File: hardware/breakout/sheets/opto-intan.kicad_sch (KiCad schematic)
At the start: 43 parts, among them J46 Intan opto out: EVT_STROBE_IN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, J47 Intan opto out: BARCODE_INTAN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, J48 Intan opto out: RWD_CMD_INTAN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, J49 Intan opto out: RWD_DLVR_INTA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, J50 Intan opto out: STIM_TRIG_INT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, J51 Intan RHS stim status in (BNC), U63 TMR 1-0511, U64 ACSL-6400-00TE, U65 ACSL-6420-00TE, U75 SN74AHCT541PW

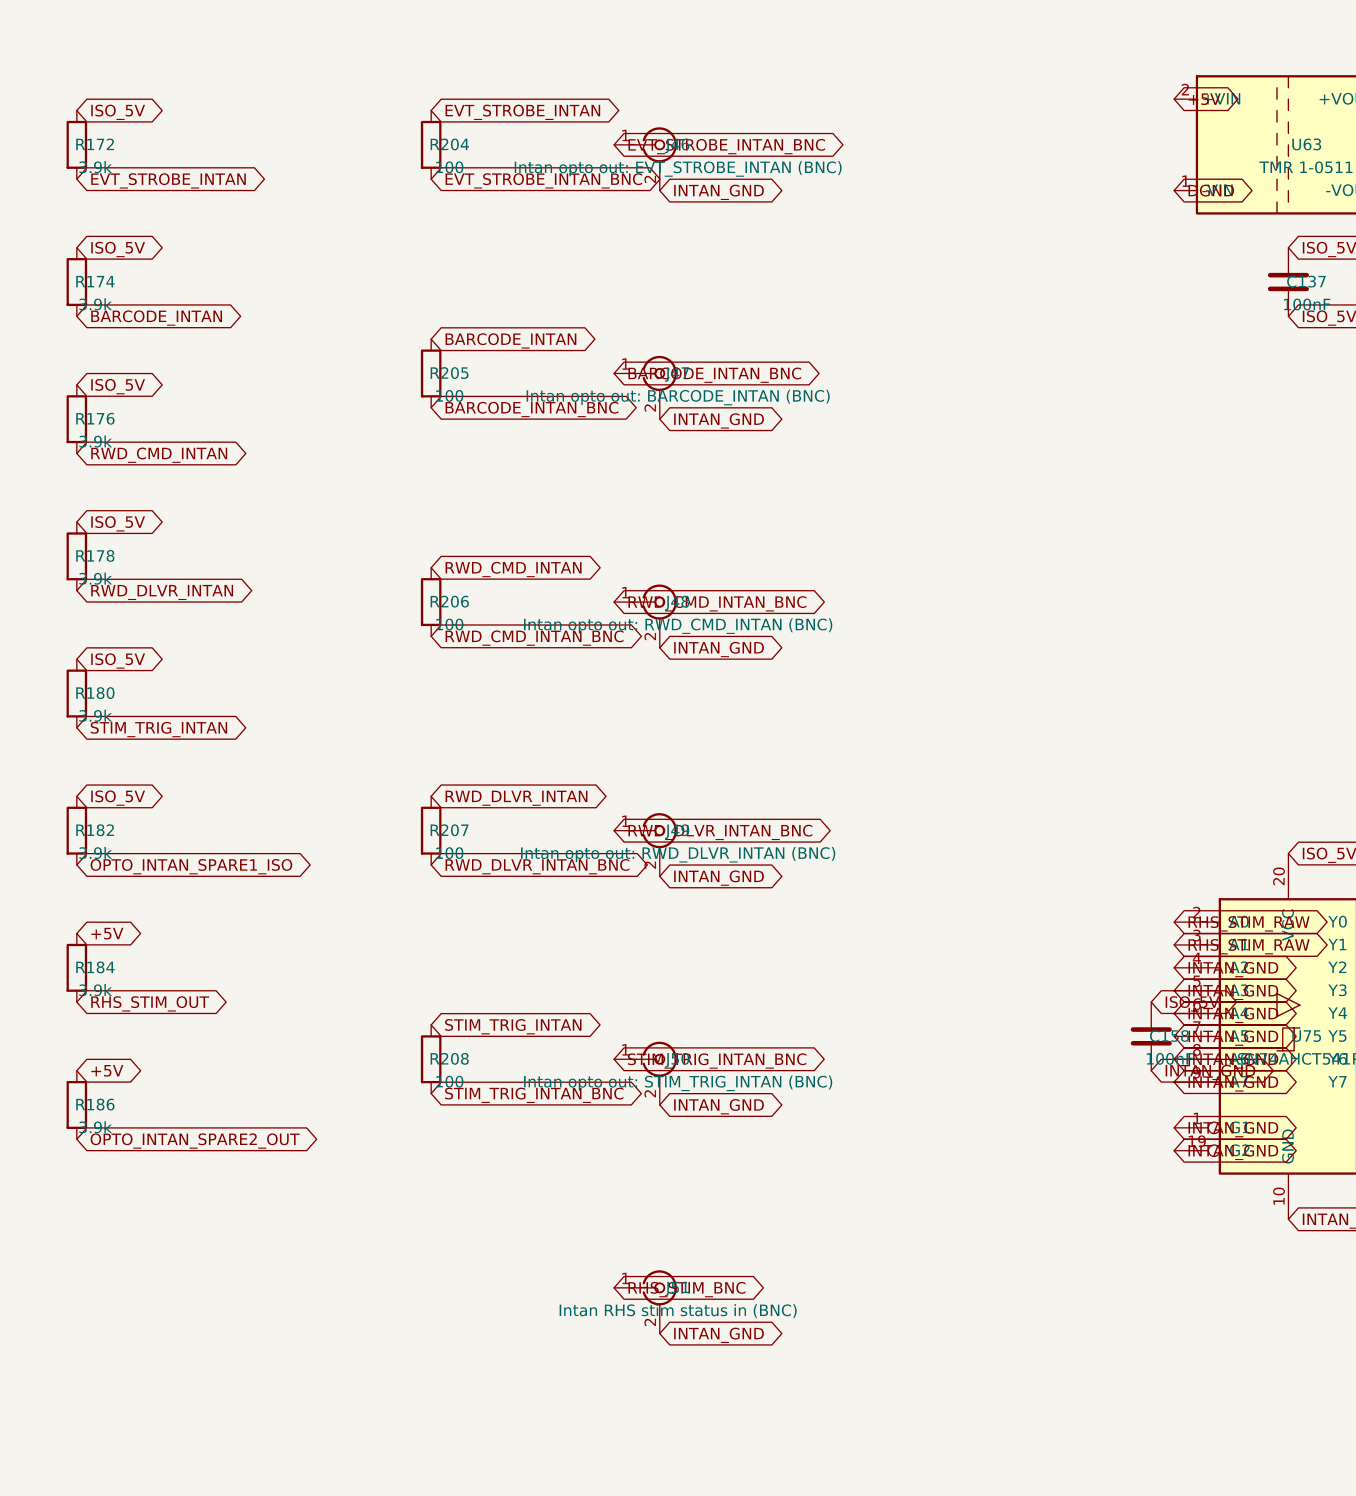
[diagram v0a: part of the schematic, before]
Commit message: fix(hardware): rebuild the connectors on their primary drawings (F6, R1, D3)
Audit step 5, the mechanical half. Three connectors changed, one of them a
fab-stopper, and none of it was visible to the netlist.

MDR68 (the fab-stopper). Rebuilt from MH drawing 3700-0121-01 rev 3.0. The
as-built footprint drilled contacts at 0.5 mm against a required 0.85 mm -- the
pins do not fit, so the board could not have been assembled -- and laid them out
as 2 rows at 2.84 mm where the drawing shows 4 staggered rows of 17 at 1.905 mm.
The 4-row stagger is what makes an 0.85 mm drill manufacturable at a 1.27 mm
mating pitch at all; the array now spans the drawing's own 41.91 mm exactly,
which is the arithmetic that confirms the reading. The claim made during the
audit that it had "no mounting holes at all" was wrong: it had two, Ø2.79 on
57.9 mm centres against the drawing's Ø2.77 on 57.93.

M12 (ruling R1). M12A_5_Panel is deleted, symbol and footprint and generator
function alike. Its contact geometry was sourced well -- IEC 61076-2-101
A-coding, cross-checked three ways -- and it made no difference, because the part
the design procures (Phoenix 1551833) terminates in AWG 22-20 wire and mounts
through the panel. It has no PCB tails, so no board-mount footprint of any
dimensions could have been right, and as built every cable insertion and every
3-4 N.m tightening loaded PCB pads directly. J1 is now a stock 5-way header where
those flying leads land; the connector stays in the order BOM as chassis
furniture.

BNC (F6). BNC_PanelMountable_Vertical puts the connector axis perpendicular to
the PCB -- a 9.65 mm barrel hole through the board -- so on a 430x240 mm board
lying flat in a 2U chassis all 31 barrels pointed at the lid rather than at the
panels. It also cost 5,654 mm2 of pad and 2,267 mm2 of removed copper on every
layer. Replaced by a right-angle dual jack built from Amphenol drawing 31-6575
rev A: 31 ports on 17 bodies, 3 spare ports, every shell still routed
individually.
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
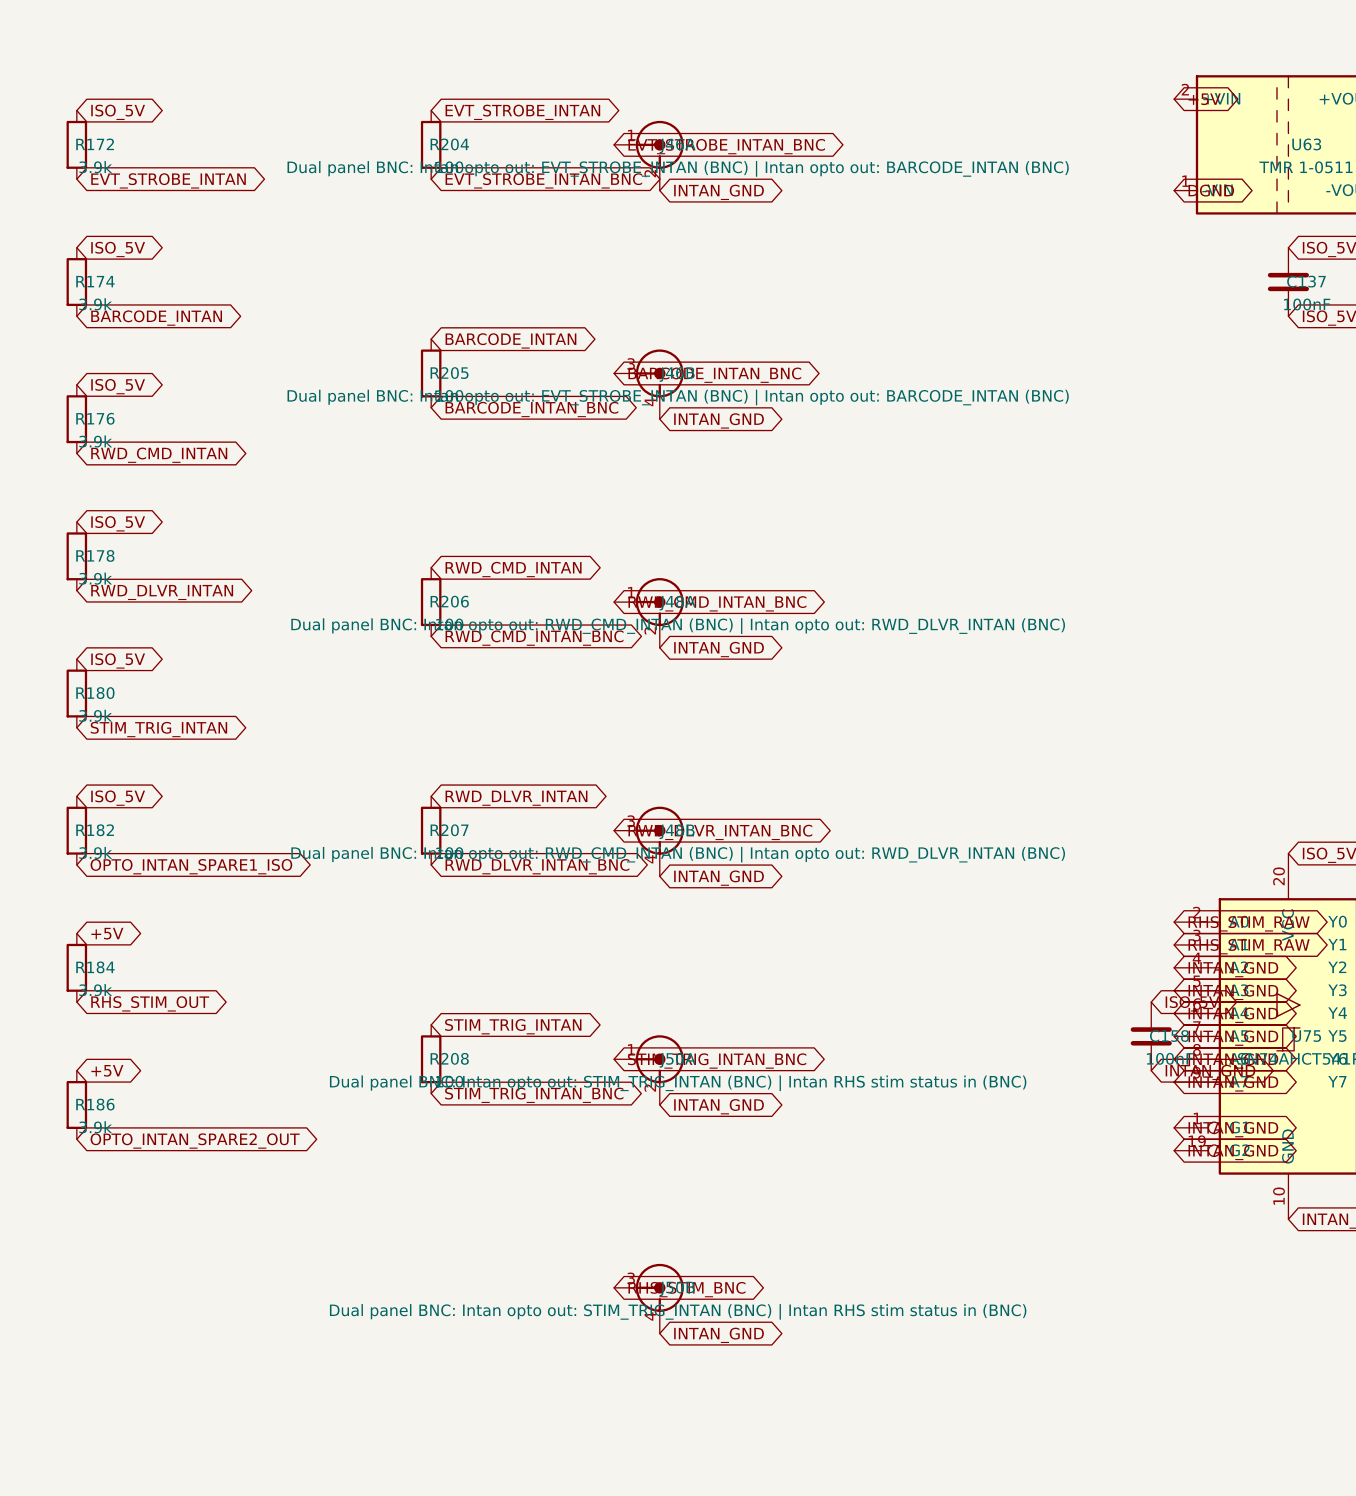
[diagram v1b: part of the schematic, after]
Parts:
- removed J46: Intan opto out: EVT_STROBE_INTAN (BNC), Connector_Coaxial:BNC_PanelMountable_Vertical, symbol Connector:Conn_Coaxial
- removed J47: Intan opto out: BARCODE_INTAN (BNC), Connector_Coaxial:BNC_PanelMountable_Vertical, symbol Connector:Conn_Coaxial
- removed J48: Intan opto out: RWD_CMD_INTAN (BNC), Connector_Coaxial:BNC_PanelMountable_Vertical, symbol Connector:Conn_Coaxial
- removed J49: Intan opto out: RWD_DLVR_INTAN (BNC), Connector_Coaxial:BNC_PanelMountable_Vertical, symbol Connector:Conn_Coaxial
- removed J50: Intan opto out: STIM_TRIG_INTAN (BNC), Connector_Coaxial:BNC_PanelMountable_Vertical, symbol Connector:Conn_Coaxial
- removed J51: Intan RHS stim status in (BNC), Connector_Coaxial:BNC_PanelMountable_Vertical, symbol Connector:Conn_Coaxial
- added J46: Dual panel BNC: Intan opto out: EVT_STROBE_INTAN 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, wl-sync:BNC_Dual_RA_Isolated, symbol wl-sync:BNC_Dual_RA_Isolated
- added J48: Dual panel BNC: Intan opto out: RWD_CMD_INTAN (BN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, wl-sync:BNC_Dual_RA_Isolated, symbol wl-sync:BNC_Dual_RA_Isolated
- added J50: Dual panel BNC: Intan opto out: STIM_TRIG_INTAN (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, wl-sync:BNC_Dual_RA_Isolated, symbol wl-sync:BNC_Dual_RA_Isolated
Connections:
- net BARCODE_INTAN_BNC: now also J46.3 (B_In)
- net EVT_STROBE_INTAN_BNC: now also J46.1 (A_In)
- net INTAN_GND: now also J46.2 (A_Ext), J46.4 (B_Ext), J48.2 (A_Ext), J48.4 (B_Ext), J50.2 (A_Ext), J50.4 (B_Ext)
- net RHS_STIM_BNC: now also J50.3 (B_In)
- net RWD_CMD_INTAN_BNC: now also J48.1 (A_In)
- net RWD_DLVR_INTAN_BNC: now also J48.3 (B_In)
- net STIM_TRIG_INTAN_BNC: now also J50.1 (A_In)
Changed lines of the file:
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@@
 	)
 	(symbol
-		(lib_id "Connector:Conn_Coaxial")
+		(lib_id "wl-sync:BNC_Dual_RA_Isolated")
 		(at 229.87 20.32 0)
 		(unit 1)
@@
 			(effects (font (size 1.27 1.27)))
 		)
-		(property "Value" "Intan opto out: EVT_STROBE_INTAN (BNC)"
+		(property "Value" "Dual panel BNC: Intan opto out: EVT_STROBE_INTAN (BNC) | Intan opto out: BARCODE_INTAN (BNC)"
 			(at 231.90200000000002 22.86 0)
 			(effects (font (size 1.27 1.27)))
 		)
-		(property "Footprint" "Connector_Coaxial:BNC_PanelMountable_Vertical"
+		(property "Footprint" "wl-sync:BNC_Dual_RA_Isolated"
 			(at 229.87 20.32 0)
 			(effects (font (size 1.27 1.27)) (hide yes))
@@
 	)
 	(symbol
-		(lib_id "Connector:Conn_Coaxial")
+		(lib_id "wl-sync:BNC_Dual_RA_Isolated")
 		(at 229.87 45.72 0)
-		(unit 1)
-		(exclude_from_sim no)
-		(in_bom yes)
-		(on_board yes)
-		(dnp no)
-		(property "Reference" "J47"
+		(unit 2)
+		(exclude_from_sim no)
+		(in_bom yes)
+		(on_board yes)
+		(dnp no)
+		(property "Reference" "J46"
 			(at 231.90200000000002 45.72 0)
 			(effects (font (size 1.27 1.27)))
 		)
-		(property "Value" "Intan opto out: BARCODE_INTAN (BNC)"
+		(property "Value" "Dual panel BNC: Intan opto out: EVT_STROBE_INTAN (BNC) | Intan opto out: BARCODE_INTAN (BNC)"
 			(at 231.90200000000002 48.26 0)
 			(effects (font (size 1.27 1.27)))
 		)
-		(property "Footprint" "Connector_Coaxial:BNC_PanelMountable_Vertical"
+		(property "Footprint" "wl-sync:BNC_Dual_RA_Isolated"
 			(at 229.87 45.72 0)
 			(effects (font (size 1.27 1.27)) (hide yes))
@@
 			(effects (font (size 1.27 1.27)) (hide yes))
 		)
-		(pin "1")
-		(pin "2")
-		(instances
-			(project "breakout"
-				(path "/d2c4d978-5db4-46d9-a1cd-a7af0aeb1700/34211e85-eb6f-485e-95d9-0458e705752e"
-					(reference "J47") (unit 1)
+		(pin "3")
+		(pin "4")
+		(instances
+			(project "breakout"
+				(path "/d2c4d978-5db4-46d9-a1cd-a7af0aeb1700/34211e85-eb6f-485e-95d9-0458e705752e"
+					(reference "J46") (unit 2)
 				)
 			)
@@
 	)
 	(symbol
-		(lib_id "Connector:Conn_Coaxial")
+		(lib_id "wl-sync:BNC_Dual_RA_Isolated")
 		(at 229.87 71.12 0)
 		(unit 1)
@@
 			(effects (font (size 1.27 1.27)))
 		)
-		(property "Value" "Intan opto out: RWD_CMD_INTAN (BNC)"
+		(property "Value" "Dual panel BNC: Intan opto out: RWD_CMD_INTAN (BNC) | Intan opto out: RWD_DLVR_INTAN (BNC)"
 			(at 231.90200000000002 73.66000000000001 0)
 			(effects (font (size 1.27 1.27)))
 		)
-		(property "Footprint" "Connector_Coaxial:BNC_PanelMountable_Vertical"
+		(property "Footprint" "wl-sync:BNC_Dual_RA_Isolated"
 			(at 229.87 71.12 0)
 			(effects (font (size 1.27 1.27)) (hide yes))
@@
 	)
 	(symbol
-		(lib_id "Connector:Conn_Coaxial")
+		(lib_id "wl-sync:BNC_Dual_RA_Isolated")
 		(at 229.87 96.52 0)
-		(unit 1)
-		(exclude_from_sim no)
-		(in_bom yes)
-		(on_board yes)
-		(dnp no)
-		(property "Reference" "J49"
+		(unit 2)
+		(exclude_from_sim no)
+		(in_bom yes)
+		(on_board yes)
+		(dnp no)
+		(property "Reference" "J48"
 			(at 231.90200000000002 96.52 0)
 			(effects (font (size 1.27 1.27)))
 		)
-		(property "Value" "Intan opto out: RWD_DLVR_INTAN (BNC)"
+		(property "Value" "Dual panel BNC: Intan opto out: RWD_CMD_INTAN (BNC) | Intan opto out: RWD_DLVR_INTAN (BNC)"
 			(at 231.90200000000002 99.06 0)
 			(effects (font (size 1.27 1.27)))
 		)
-		(property "Footprint" "Connector_Coaxial:BNC_PanelMountable_Vertical"
+		(property "Footprint" "wl-sync:BNC_Dual_RA_Isolated"
 			(at 229.87 96.52 0)
 			(effects (font (size 1.27 1.27)) (hide yes))
@@
 			(effects (font (size 1.27 1.27)) (hide yes))
 		)
-		(pin "1")
-		(pin "2")
-		(instances
-			(project "breakout"
-				(path "/d2c4d978-5db4-46d9-a1cd-a7af0aeb1700/34211e85-eb6f-485e-95d9-0458e705752e"
-					(reference "J49") (unit 1)
+		(pin "3")
+		(pin "4")
+		(instances
+			(project "breakout"
+				(path "/d2c4d978-5db4-46d9-a1cd-a7af0aeb1700/34211e85-eb6f-485e-95d9-0458e705752e"
+					(reference "J48") (unit 2)
 				)
 			)
@@
 	)
 	(symbol
-		(lib_id "Connector:Conn_Coaxial")
+		(lib_id "wl-sync:BNC_Dual_RA_Isolated")
 		(at 229.87 121.92 0)
 		(unit 1)
@@
 			(effects (font (size 1.27 1.27)))
 		)
-		(property "Value" "Intan opto out: STIM_TRIG_INTAN (BNC)"
+		(property "Value" "Dual panel BNC: Intan opto out: STIM_TRIG_INTAN (BNC) | Intan RHS stim status in (BNC)"
 			(at 231.90200000000002 124.46000000000001 0)
 			(effects (font (size 1.27 1.27)))
 		)
-		(property "Footprint" "Connector_Coaxial:BNC_PanelMountable_Vertical"
+		(property "Footprint" "wl-sync:BNC_Dual_RA_Isolated"
 			(at 229.87 121.92 0)
 			(effects (font (size 1.27 1.27)) (hide yes))
@@
 	)
 	(symbol
-		(lib_id "Connector:Conn_Coaxial")
+		(lib_id "wl-sync:BNC_Dual_RA_Isolated")
 		(at 229.87 147.32 0)
-		(unit 1)
-		(exclude_from_sim no)
-		(in_bom yes)
-		(on_board yes)
-		(dnp no)
-		(property "Reference" "J51"
+		(unit 2)
+		(exclude_from_sim no)
+		(in_bom yes)
+		(on_board yes)
+		(dnp no)
+		(property "Reference" "J50"
 			(at 231.90200000000002 147.32 0)
 			(effects (font (size 1.27 1.27)))
 		)
-		(property "Value" "Intan RHS stim status in (BNC)"
+		(property "Value" "Dual panel BNC: Intan opto out: STIM_TRIG_INTAN (BNC) | Intan RHS stim status in (BNC)"
 			(at 231.90200000000002 149.85999999999999 0)
 			(effects (font (size 1.27 1.27)))
 		)
-		(property "Footprint" "Connector_Coaxial:BNC_PanelMountable_Vertical"
+		(property "Footprint" "wl-sync:BNC_Dual_RA_Isolated"
 			(at 229.87 147.32 0)
 			(effects (font (size 1.27 1.27)) (hide yes))
@@
 			(effects (font (size 1.27 1.27)) (hide yes))
 		)
-		(pin "1")
-		(pin "2")
-		(instances
-			(project "breakout"
-				(path "/d2c4d978-5db4-46d9-a1cd-a7af0aeb1700/34211e85-eb6f-485e-95d9-0458e705752e"
-					(reference "J51") (unit 1)
-				)
-			)
+		(pin "3")
+		(pin "4")
+		(instances
+			(project "breakout"
+				(path "/d2c4d978-5db4-46d9-a1cd-a7af0aeb1700/34211e85-eb6f-485e-95d9-0458e705752e"
+					(reference "J50") (unit 2)
+				)
+			)
